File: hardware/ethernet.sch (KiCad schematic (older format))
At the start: 54 parts

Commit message: Added 3v3 sync buck smps
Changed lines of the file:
@@
 NoConn ~ 8300 5700
 Wire Wire Line
-	6600 4600 6950 4600
-Wire Wire Line
-	6950 4600 7200 4600
-Wire Wire Line
-	7200 4600 7200 4700
-Wire Wire Line
-	7200 4700 7200 4800
-Wire Wire Line
-	7200 4800 7200 4900
+	6600 4600 7200 4600
+Wire Wire Line
+	7200 4600 7200 4900
 Wire Wire Line
 	7200 4700 7300 4700
@@
 	8600 6000 8600 5900
 Wire Wire Line
-	8300 6000 8400 6000
-Wire Wire Line
-	8400 6000 8600 6000
-Wire Wire Line
-	8600 6000 8650 6000
+	8300 6000 8650 6000
 Wire Wire Line
 	8650 6000 8650 6100
@@
 	7200 6000 7300 6000
 Wire Wire Line
-	7200 5800 7200 5900
-Wire Wire Line
-	7200 5900 7200 6000
-Wire Wire Line
-	7200 6000 7200 6050
+	7200 5800 7200 6050
 Wire Wire Line
 	7300 5900 7200 5900
@@
 	8400 4600 8550 4600
 Wire Wire Line
-	8300 4900 8350 4900
-Wire Wire Line
-	8350 4900 8550 4900
-Wire Wire Line
-	8350 4900 8350 5000
-Wire Wire Line
-	8350 5000 8350 5100
+	8300 4900 8550 4900
+Wire Wire Line
+	8350 4900 8350 5100
 Wire Wire Line
 	8350 5000 8300 5000
 Connection ~ 8350 4900
 Wire Wire Line
-	8300 5100 8350 5100
-Wire Wire Line
-	8350 5100 8700 5100
+	8300 5100 8700 5100
 Connection ~ 8350 5000
 Connection ~ 8350 5100
 Wire Wire Line
-	9300 5100 9400 5100
-Wire Wire Line
-	9400 5100 9600 5100
-Wire Wire Line
-	9600 5100 10000 5100
-Wire Wire Line
-	10000 5100 10400 5100
+	9300 5100 10400 5100
 Wire Wire Line
 	9400 5100 9400 5200
@@
 $EndComp
 Wire Wire Line
-	1100 6700 1250 6700
-Wire Wire Line
-	1250 6700 1400 6700
+	1100 6700 1400 6700
 Wire Wire Line
 	1100 6450 1100 6500
@@
 	1400 6450 1400 6500
 Wire Wire Line
-	1100 6250 1250 6250
-Wire Wire Line
-	1250 6250 1400 6250
+	1100 6250 1400 6250
 Wire Wire Line
 	1250 6250 1250 6100
 Wire Wire Line
-	1250 6100 2100 6100
-Wire Wire Line
-	2100 6100 2700 6100
-Wire Wire Line
-	2700 6100 3550 6100
-Wire Wire Line
-	3550 6100 3850 6100
-Wire Wire Line
-	3850 6100 3950 6100
+	1250 6100 3950 6100
 Connection ~ 1250 6250
 Wire Wire Line
 	1250 6700 1250 6800
 Wire Wire Line
-	3200 6800 2950 6800
-Wire Wire Line
-	2950 6800 2700 6800
-Wire Wire Line
-	2700 6800 2100 6800
-Wire Wire Line
-	2100 6800 1250 6800
+	3200 6800 1250 6800
 Connection ~ 1250 6700
 Text Label 1050 6500 2    60   ~ 0
@@
 Connection ~ 1400 6500
 Wire Wire Line
-	1950 6700 2100 6700
-Wire Wire Line
-	2100 6700 2250 6700
+	1950 6700 2250 6700
 Wire Wire Line
 	2100 6800 2100 6700
 Connection ~ 2100 6700
 Wire Wire Line
-	1950 6250 2100 6250
-Wire Wire Line
-	2100 6250 2250 6250
+	1950 6250 2250 6250
 Wire Wire Line
 	2100 6100 2100 6250
@@
 	3950 6200 3950 6300
 Wire Wire Line
-	3200 6200 3200 6600
-Wire Wire Line
-	3200 6600 3200 6800
+	3200 6200 3200 6800
 Wire Wire Line
 	3200 6200 3950 6200
@@
 	4750 6200 4900 6200
 Wire Wire Line
-	4900 6200 4900 6500
-Wire Wire Line
-	4900 6500 4900 6600
+	4900 6200 4900 6600
 Wire Wire Line
 	4900 6500 4750 6500
@@
 	2100 1550 2100 1650
 Wire Wire Line
-	2000 1650 2100 1650
-Wire Wire Line
-	2100 1650 2150 1650
-Wire Wire Line
-	2150 1650 2200 1650
+	2000 1650 2200 1650
 Connection ~ 2100 1650
 Text Label 2300 1950 0    60   ~ 0
@@
 	2250 1950 2250 1850
 Wire Wire Line
-	2000 1950 2200 1950
-Wire Wire Line
-	2200 1950 2250 1950
-Wire Wire Line
-	2250 1950 2300 1950
+	2000 1950 2300 1950
 Connection ~ 2250 1950
 $Comp
@@
 $EndComp
 Wire Wire Line
-	2700 1350 2750 1350
-Wire Wire Line
-	2750 1350 2850 1350
-Wire Wire Line
-	2700 1750 2800 1750
-Wire Wire Line
-	2800 1750 2850 1750
+	2700 1350 2850 1350
+Wire Wire Line
+	2700 1750 2850 1750
 Connection ~ 2800 1750
 Connection ~ 2750 1350
@@
 	2350 2900 2350 2950
 Wire Wire Line
-	2150 2950 2350 2950
-Wire Wire Line
-	2350 2950 2450 2950
-Wire Wire Line
-	2450 2950 2550 2950
-Wire Wire Line
-	2550 2950 2750 2950
+	2150 2950 2750 2950
 Wire Wire Line
 	2450 2950 2450 3000
@@
 $EndComp
 Wire Wire Line
-	6250 1200 6450 1200
-Wire Wire Line
-	6450 1200 6850 1200
+	6250 1200 6850 1200
 Connection ~ 6450 1200
 $Comp
@@
 $EndComp
 Wire Wire Line
-	6500 900  6600 900
-Wire Wire Line
-	6600 900  6650 900
+	6500 900  6650 900
 Wire Wire Line
 	6600 900  6600 1000
@@
 	7050 2850 7050 2900
 Wire Wire Line
-	6900 2900 7050 2900
-Wire Wire Line
-	7050 2900 7150 2900
+	6900 2900 7150 2900
 Connection ~ 7050 2900
 $Comp
@@
 $EndComp
 Wire Wire Line
-	6900 3200 7050 3200
-Wire Wire Line
-	7050 3200 7150 3200
+	6900 3200 7150 3200
 Connection ~ 7050 3200
 $Comp
@@
 	7750 2850 7750 2900
 Wire Wire Line
-	7600 2900 7750 2900
-Wire Wire Line
-	7750 2900 7850 2900
+	7600 2900 7850 2900
 Connection ~ 7750 2900
 $Comp
@@
 $EndComp
 Wire Wire Line
-	7600 3200 7750 3200
-Wire Wire Line
-	7750 3200 7850 3200
+	7600 3200 7850 3200
 Connection ~ 7750 3200
 Text Notes 6750 3600 0    60   ~ 0
@@
 $EndComp
 Wire Wire Line
-	6250 2300 6450 2300
-Wire Wire Line
-	6450 2300 6850 2300
+	6250 2300 6850 2300
 Wire Wire Line
 	6450 2300 6450 2350
 Wire Wire Line
-	6250 2200 6650 2200
-Wire Wire Line
-	6650 2200 6850 2200
+	6250 2200 6850 2200
 Wire Wire Line
 	6650 2200 6650 2350
@@
 Connection ~ 6650 2200
 Wire Wire Line
-	6450 2650 6550 2650
-Wire Wire Line
-	6550 2650 6650 2650
+	6450 2650 6650 2650
 Wire Wire Line
 	6550 2650 6550 2700
@@
 $EndComp
 Wire Wire Line
-	8050 1800 8550 1800
-Wire Wire Line
-	8550 1800 8700 1800
+	8050 1800 8700 1800
 Connection ~ 8550 1800
 Wire Wire Line
@@
 	8450 2100 8500 2100
 Wire Wire Line
-	8050 2400 9300 2400
-Wire Wire Line
-	9300 2400 9400 2400
-Wire Wire Line
-	9400 2400 9500 2400
+	8050 2400 9500 2400
 $Comp
 L D D?
@@
 Connection ~ 9400 2400
 Wire Wire Line
-	9300 2100 9400 2100
-Wire Wire Line
-	9400 2100 9500 2100
+	9300 2100 9500 2100
 Wire Wire Line
 	9400 2100 9400 2050

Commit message: stm32 psu and SWD programming
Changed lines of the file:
@@
 	1250 6700 1250 6800
 Wire Wire Line
-	3200 6800 1250 6800
+	1250 6800 3200 6800
 Connection ~ 1250 6700
 Text Label 1050 6500 2    60   ~ 0
@@
 	3950 6200 3950 6300
 Wire Wire Line
-	3200 6200 3200 6800
+	3200 6800 3200 6200
 Wire Wire Line
 	3200 6200 3950 6200
@@
 	2000 1850 2250 1850
 Wire Wire Line
-	2250 1950 2250 1850
+	2250 1850 2250 1950
 Wire Wire Line
 	2000 1950 2300 1950

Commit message: Firing matrix and CC SMPS
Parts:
- removed C? (x3): 22u, agg:1206, symbol C
- added C217, C222, C223: 22u, agg:1206, symbol C
- C214: renamed from C?; Farnell 2118135 -> 1797010
- R210: renamed from R?; Farnell 2059627 -> 2303192
- gave numbers to parts that had none: 49
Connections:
- net +6V: now also C222.1, C223.1
- net 3v3: now also C217.1
- net GND: now also C217.2, C222.2, C223.2

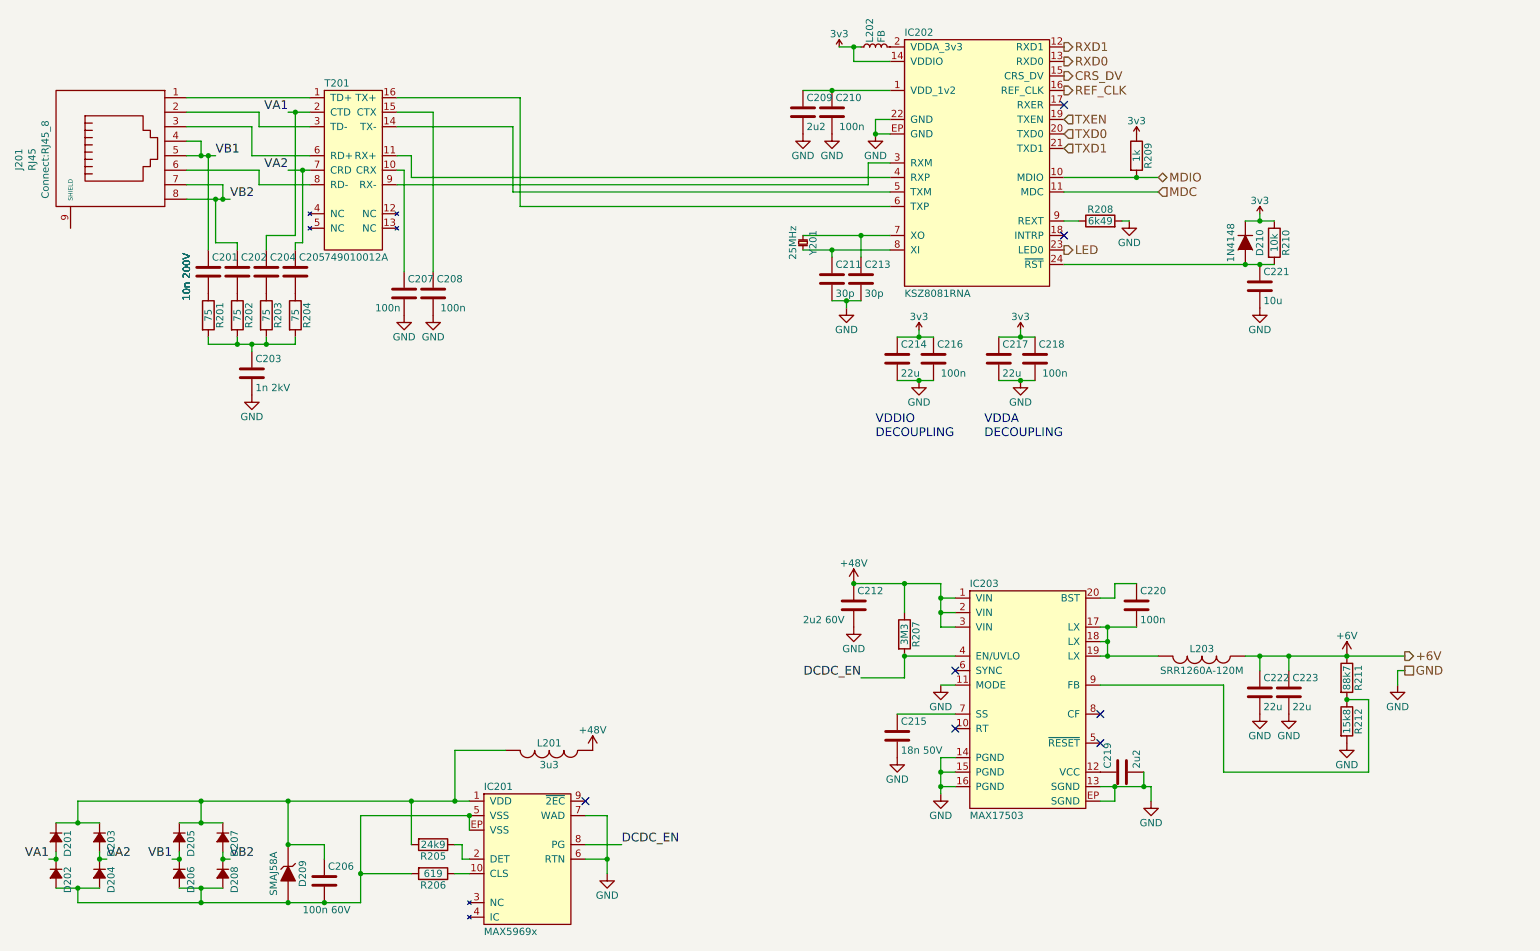
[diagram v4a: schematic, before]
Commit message: aux power, test points
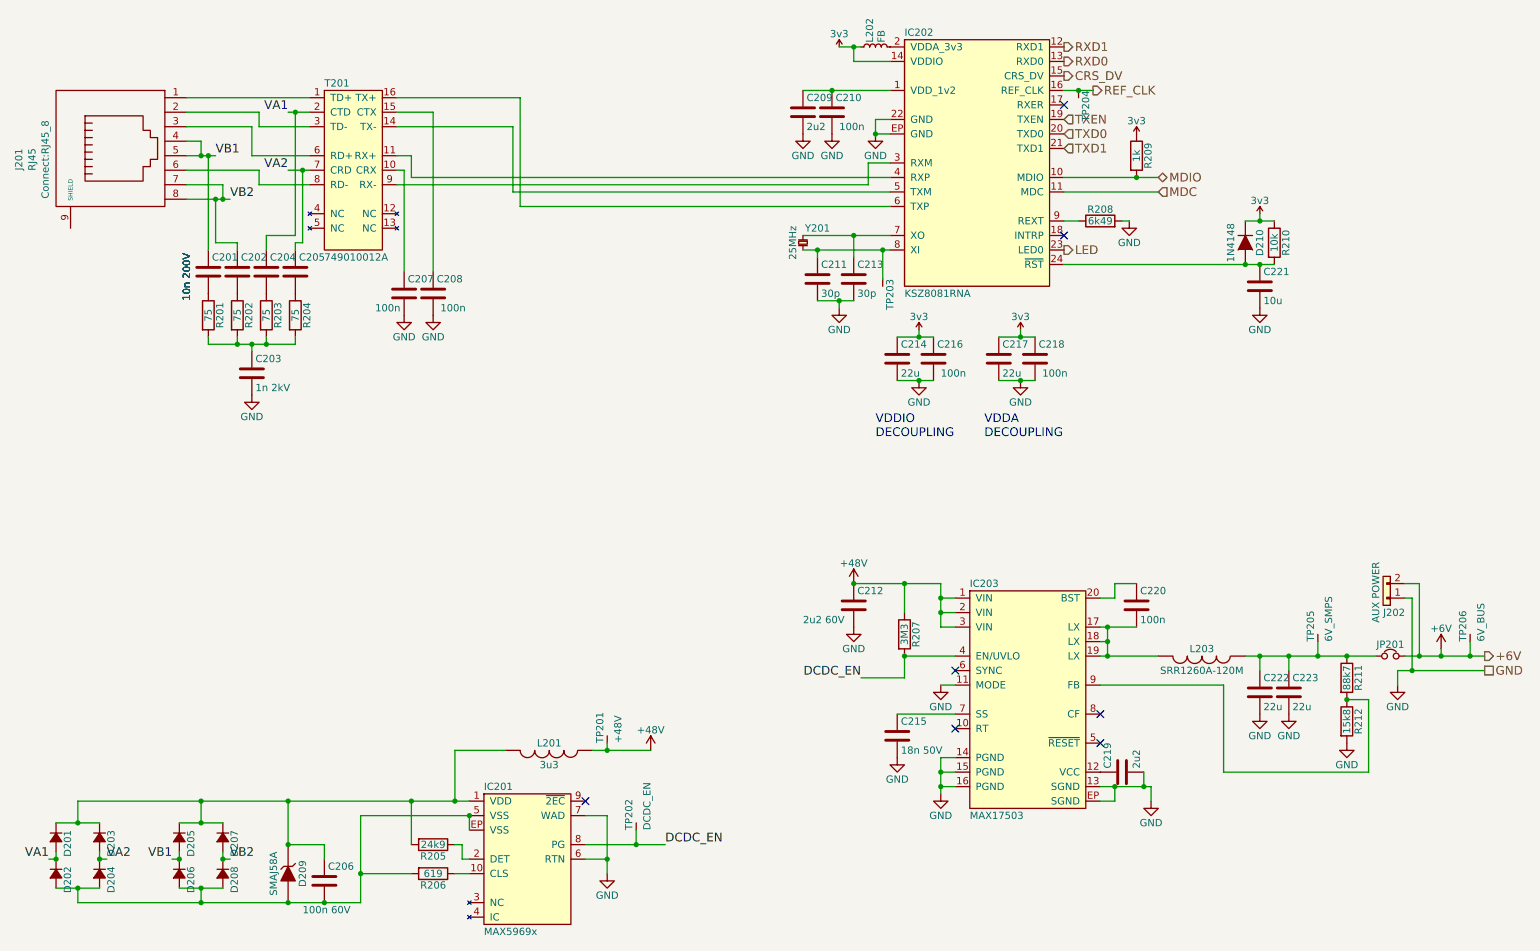
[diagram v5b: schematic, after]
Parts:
- added J202: AUX POWER, hardware:Minipow, symbol CONN_01x02
- added JP201: Jumper_NC_Small, hardware:jump_NC, symbol Jumper_NC_Small
- added TP201: +48V, hardware:Test_point_mini, symbol TESTPAD
- added TP202: DCDC_EN, hardware:Test_point_mini, symbol TESTPAD
- added TP203: 25MHz_XTAL, agg:TESTPAD, symbol TESTPAD
- added TP204: 50MHz_CLK, agg:TESTPAD, symbol TESTPAD
- added TP205: 6V_SMPS, hardware:Test_point_mini, symbol TESTPAD
- added TP206: 6V_BUS, hardware:Test_point_mini, symbol TESTPAD
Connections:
- net +48V: now also TP201.1 (TP)
- net +6V: now also J202.2, JP201.2, TP206.1 (TP); no longer C222.1, C223.1, L203.1, R211.1
- net DCDC_EN: now also TP202.1 (TP)
- net GND: now also J202.1
- net REF_CLK: now also TP204.1 (TP)
- net at C211.1, IC202.8 (XI), Y201.2: now also TP203.1 (TP)
- new net: C222.1, C223.1, JP201.1, L203.1, R211.1, TP205.1 (TP)
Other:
- moved on the sheet: C211, C213

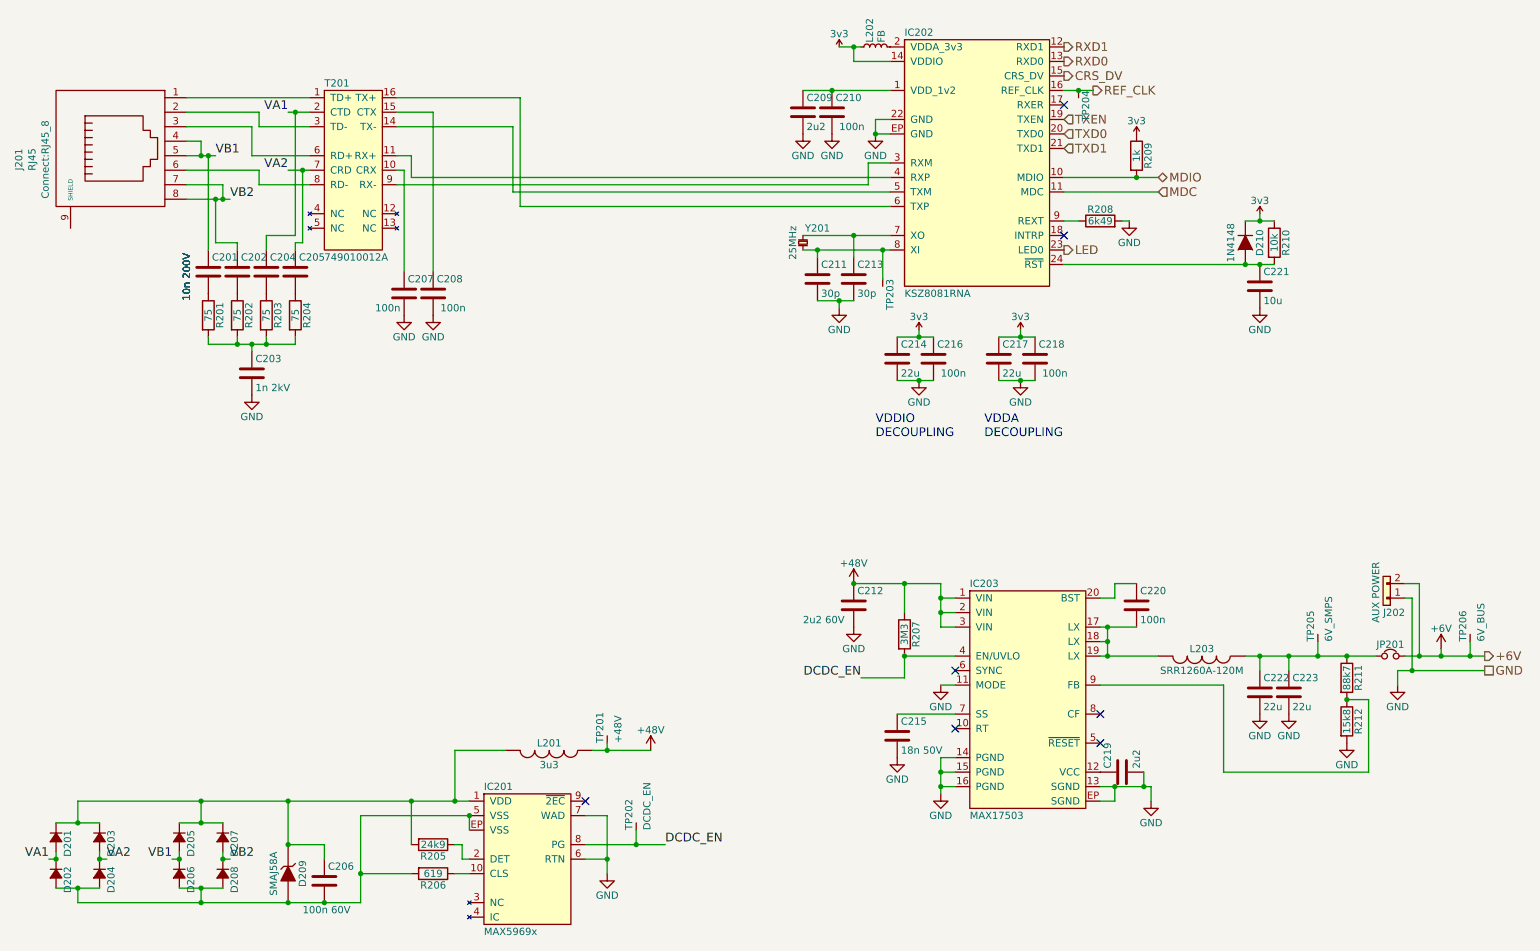
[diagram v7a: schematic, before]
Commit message: LEDs, ethernet jack
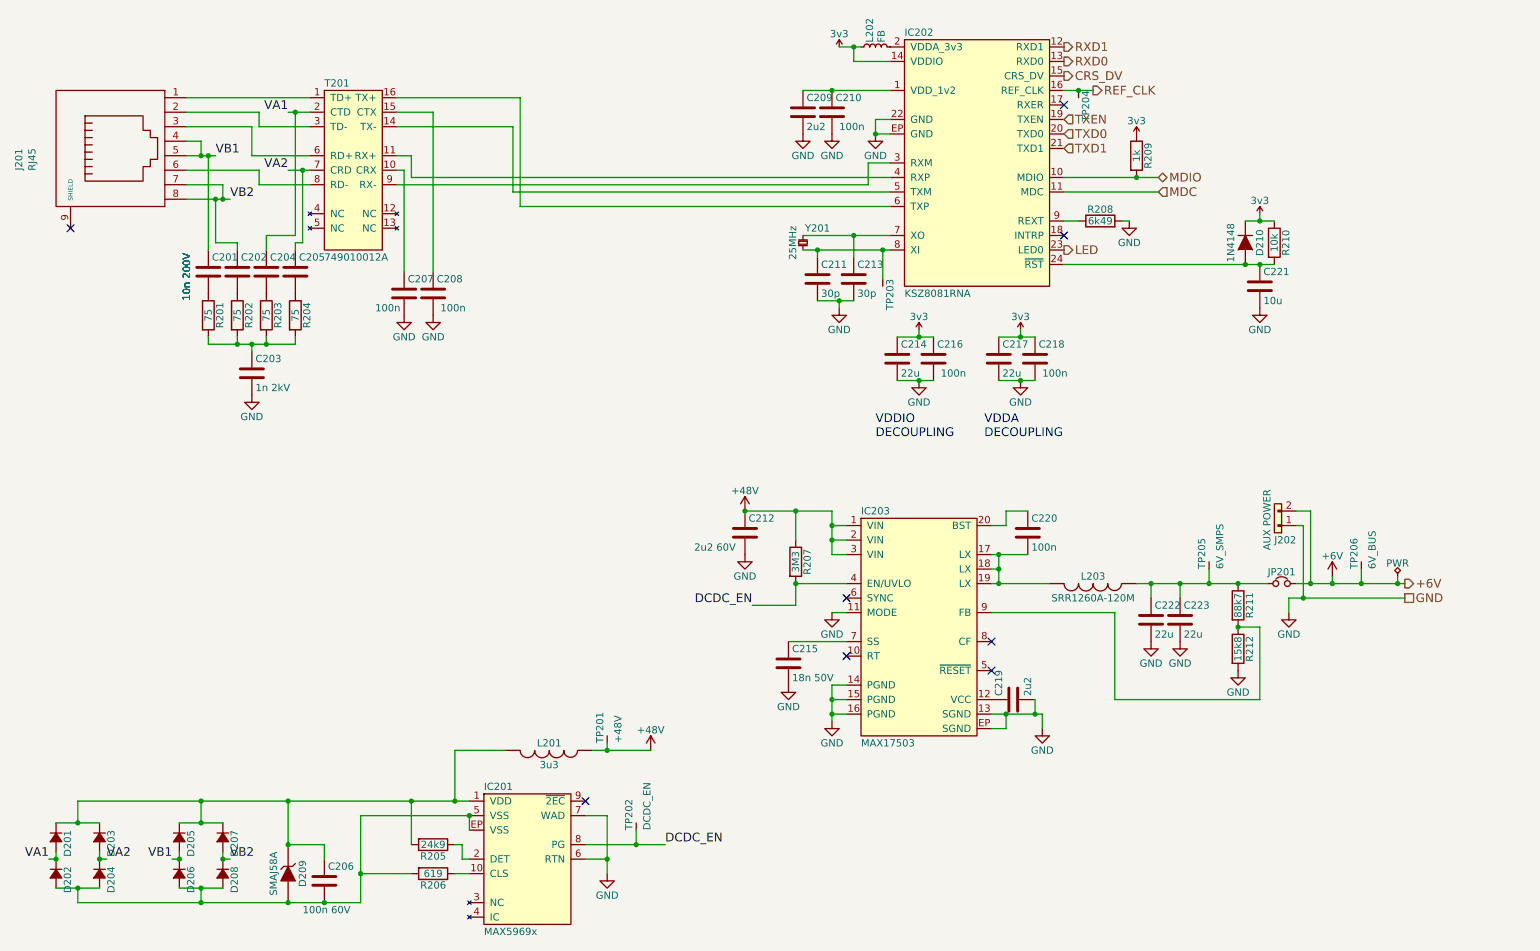
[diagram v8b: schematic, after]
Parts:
- J201: footprint Connect:RJ45_8 -> hardware:RJHSE5380; Farnell (none) -> 1860580
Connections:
- no-connect marks 7 -> 8
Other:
- moved on the sheet: C212, C215, C219, C220, C222, C223, IC203, J202, JP201, L203, R207, R211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
